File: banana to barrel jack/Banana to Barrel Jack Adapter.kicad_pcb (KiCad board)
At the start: 2 copper layers, 34.3 x 26.6 mm, 29 parts, among them J1 USB_A, J2 Positive, J3 Negative, J4 Data

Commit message: Zone Relief DRC error in PCB
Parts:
- removed ? (x7): , 
- removed J4: Data, Connector_PinHeader_2.54mm:PinHeader_1x02_P2.54mm_Vertical
- removed the REF** at (133.1, 98.6)
- removed the REF** at (127.3, 99.5)
- removed the REF** at (133.1, 100.8)
- removed the REF** at (133.1, 102.0)
- removed the REF** at (129.6, 99.5)
- removed the REF** at (131.9, 99.5)
- removed the REF** at (133.1, 97.6)
- removed the REF** at (133.1, 99.6)
- removed the REF** at (130.8, 99.5)
- removed the REF** at (133.1, 103.1)
- removed the REF** at (133.1, 96.5)
- removed the REF** at (128.5, 99.5)
- removed the REF** at (126.1, 99.5)
- added D2: Green, LED_SMD:LED_1206_3216Metric_Pad1.42x1.75mm_HandSolder, B.Cu at (146.8, 96.9)
- added R2: 1k, Resistor_SMD:R_1206_3216Metric_Pad1.30x1.75mm_HandSolder, B.Cu at (146.8, 102.3)
- added REF**: Symbol_Barrel_Polarity, Symbol:Symbol_Barrel_Polarity, F.Cu at (151.2, 106.4)
- added REF**: Symbol_Barrel_Polarity, Symbol:Symbol_Barrel_Polarity, B.Cu at (151.2, 106.2)
- J1: value USB_A -> Barrel_Jack_Switch; footprint My Libraries:USB_A_GCT_USB1125 -> Connector_BarrelJack:BarrelJack_GCT_DCJ200-10-A_Horizontal
- moved J1 4.44 mm to (151.7, 98.8)
- moved D3 1.93 mm to (154.8, 99.5)
- renumbered D2 to D3
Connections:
- J1 pad 2: Net-(J1-D-) -> GND
- J1 pad 3: Net-(J1-D+) -> GND
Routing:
- net /Positive: track 0.00 -> 7.05 mm
- net Net-(J1-D-): track 3.53 -> 0.00 mm
- net Net-(J1-D+): track 3.52 -> 0.00 mm

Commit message: 0 DRC before changing zones for positive
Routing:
- net /Positive: track 7.05 -> 0.00 mm
- net Net-(D2-A): track 0.00 -> 2.31 mm
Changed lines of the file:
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@@
 		)
 		(model "${KICAD8_3DMODEL_DIR}/Connector_BarrelJack.3dshapes/BarrelJack_GCT_DCJ200-10-A_Horizontal.wrl"
+			(hide yes)
 			(offset
 				(xyz 0 0 0)
@@
 			)
 		)
+		(model "${KICAD8_3DMODEL_DIR}/Connector_BarrelJack.3dshapes/BarrelJack_Horizontal.step"
+			(offset
+				(xyz 0 0 0)
+			)
+			(scale
+				(xyz 1 1 1)
+			)
+			(rotate
+				(xyz 0 0 -90)
+			)
+		)
 	)
 	(footprint "Connector_PinHeader_2.54mm:PinHeader_1x01_P2.54mm_Vertical"
@@
 		)
 	)
+	(gr_rect
+		(start 127.75 95.75)
+		(end 129.05 95.65)
+		(stroke
+			(width 0)
+			(type solid)
+		)
+		(fill solid)
+		(layer "B.SilkS")
+	)
+	(gr_rect
+		(start 127.75 96.85)
+		(end 129.05 96.75)
+		(stroke
+			(width 0)
+			(type solid)
+		)
+		(fill solid)
+		(layer "B.SilkS")
+	)
 	(gr_line
 		(start 131.725 95.925)
@@
 		(layer "B.SilkS")
 	)
+	(gr_rect
+		(start 127.75 96.825)
+		(end 128.2 95.675)
+		(stroke
+			(width 0)
+			(type solid)
+		)
+		(fill solid)
+		(layer "B.SilkS")
+	)
+	(gr_rect
+		(start 146.85 90.9)
+		(end 147.55 88.75)
+		(stroke
+			(width 0)
+			(type solid)
+		)
+		(fill solid)
+		(layer "B.SilkS")
+	)
+	(gr_rect
+		(start 128.55 96.825)
+		(end 129.05 95.675)
+		(stroke
+			(width 0)
+			(type solid)
+		)
+		(fill solid)
+		(layer "B.SilkS")
+	)
 	(gr_line
 		(start 131.725 102.85)
@@
 		(layer "B.SilkS")
 	)
+	(gr_rect
+		(start 148.1 90.9)
+		(end 148.8 88.75)
+		(stroke
+			(width 0)
+			(type solid)
+		)
+		(fill solid)
+		(layer "B.SilkS")
+	)
+	(gr_rect
+		(start 146.85 90.9)
+		(end 148.75 90.7)
+		(stroke
+			(width 0)
+			(type solid)
+		)
+		(fill solid)
+		(layer "B.SilkS")
+	)
+	(gr_rect
+		(start 146.85 88.95)
+		(end 148.75 88.75)
+		(stroke
+			(width 0)
+			(type solid)
+		)
+		(fill solid)
+		(layer "B.SilkS")
+	)
 	(gr_line
 		(start 131.725 102.825)
@@
 		(layer "B.SilkS")
 	)
+	(gr_rect
+		(start 128.6 95.675)
+		(end 129.05 96.825)
+		(stroke
+			(width 0)
+			(type solid)
+		)
+		(fill solid)
+		(layer "F.SilkS")
+	)
+	(gr_rect
+		(start 146.9 90.7)
+		(end 148.8 90.9)
+		(stroke
+			(width 0)
+			(type solid)
+		)
+		(fill solid)
+		(layer "F.SilkS")
+	)
+	(gr_rect
+		(start 127.75 95.65)
+		(end 129.05 95.75)
+		(stroke
+			(width 0)
+			(type solid)
+		)
+		(fill solid)
+		(layer "F.SilkS")
+	)
+	(gr_rect
+		(start 127.75 95.675)
+		(end 128.25 96.825)
+		(stroke
+			(width 0)
+			(type solid)
+		)
+		(fill solid)
+		(layer "F.SilkS")
+	)
 	(gr_line
 		(start 139.575 103.075)
@@
 		(layer "F.SilkS")
 	)
+	(gr_rect
+		(start 127.75 96.75)
+		(end 129.05 96.85)
+		(stroke
+			(width 0)
+			(type solid)
+		)
+		(fill solid)
+		(layer "F.SilkS")
+	)
 	(gr_circle
 		(center 131.75 103.025)
@@
 		(layer "F.SilkS")
 	)
+	(gr_rect
+		(start 146.9 88.75)
+		(end 148.8 88.95)
+		(stroke
+			(width 0)
+			(type solid)
+		)
+		(fill solid)
+		(layer "F.SilkS")
+	)
 	(gr_line
 		(start 139.575 103.075)
@@
 		(layer "F.SilkS")
 	)
+	(gr_rect
+		(start 148.1 88.75)
+		(end 148.8 90.9)
+		(stroke
+			(width 0)
+			(type solid)
+		)
+		(fill solid)
+		(layer "F.SilkS")
+	)
 	(gr_line
 		(start 139.4 103.25)
@@
 		(layer "F.SilkS")
 	)
+	(gr_rect
+		(start 146.85 88.75)
+		(end 147.55 90.9)
+		(stroke
+			(width 0)
+			(type solid)
+		)
+		(fill solid)
+		(layer "F.SilkS")
+	)
 	(gr_line
 		(start 139.4 102.9)
@@
 	)
 	(gr_text "-"
-		(at 128.4895 96.26765 -90)
+		(at 128.4895 96.25 -90)
 		(layer "B.SilkS" knockout)
 		(effects
@@
 	)
 	(gr_text "+"
-		(at 128.4895 102.703 0)
+		(at 128.4895 102.65 0)
 		(layer "B.SilkS" knockout)
 		(effects
@@
 	)
 	(gr_text "-"
-		(at 149.1742 91.166995 90)
+		(at 148.85 91.15 90)
 		(layer "F.SilkS" knockout)
 		(effects
@@
 	)
 	(gr_text "+"
-		(at 146.761105 110.1789 0)
+		(at 146.55 110.1789 0)
 		(layer "F.SilkS" knockout)
 		(effects
@@
 	)
 	(gr_text "-"
-		(at 128.4895 96.221425 90)
+		(at 128.35 96.25 90)
 		(layer "F.SilkS" knockout)
 		(effects
@@
 		(net 1)
 	)
-	(segment
-		(start 149.89325 100.6458)
-		(end 153.0255 100.6458)
-		(width 0.25)
-		(layer "F.Cu")
-		(net 2)
-	)
-	(segment
-		(start 153.0255 100.6458)
-		(end 153.3065 100.3648)
-		(width 0.25)
-		(layer "F.Cu")
-		(net 2)
-	)
-	(segment
-		(start 149.89325 98.1058)
-		(end 153.0475 98.1058)
-		(width 0.25)
-		(layer "F.Cu")
-		(net 2)
-	)
-	(segment
-		(start 153.0475 98.1058)
-		(end 153.3065 98.3648)
-		(width 0.25)
-		(layer "F.Cu")
-		(net 2)
-	)
 	(via
 		(at 144.8562 110.53572)
@@
 		(net 3)
 	)
+	(segment
+		(start 146.79 98.4075)
+		(end 146.79 100.72)
+		(width 0.5)
+		(layer "B.Cu")
+		(net 4)
+	)
 	(zone
 		(net 2)
@@
 		)
 	)
+	(group ""
+		(members "03433355-6bb3-446d-9a6d-a2e5b72d6f9c" "07b327e9-676c-4b22-8802-34a8a017ee86"
+			"812e787f-b3ed-41a6-bb3a-bdb902afadbf" "8b55572f-fa6a-4e7c-b22f-9cf51528f95c"
+		)
+	)
+	(group ""
+		(members "876096bc-b1d5-4e9a-9cdb-3daaf280bf9d" "9402d68d-7a4b-4ece-86ce-f0ebfa78f54e"
+			"a5ec77df-c86e-444f-92c5-92dc659a62b3" "b2f959b1-7101-4a8c-b801-1e8fdb9a2005"
+		)
+	)
+	(group ""
+		(members "22873648-8d8c-450a-9397-42385f8aac2b" "9b107eb4-2d82-42f6-b674-1bb251eae402"
+			"c5bfd072-bf1a-4381-a8b1-2d2add5322a2" "e6739268-a3a3-4171-aaab-85ea9d387f7c"
+		)
+	)
+	(group ""
+		(members "12e7e9ea-4806-45f0-af63-483ef2b5ac83" "32d8726d-c00d-4061-87aa-49370713e9ea"
+			"35eebb64-d20b-4ada-b715-29849750b198" "722da3e9-53a3-4bcb-9cbf-1dace17913f2"
+		)
+	)

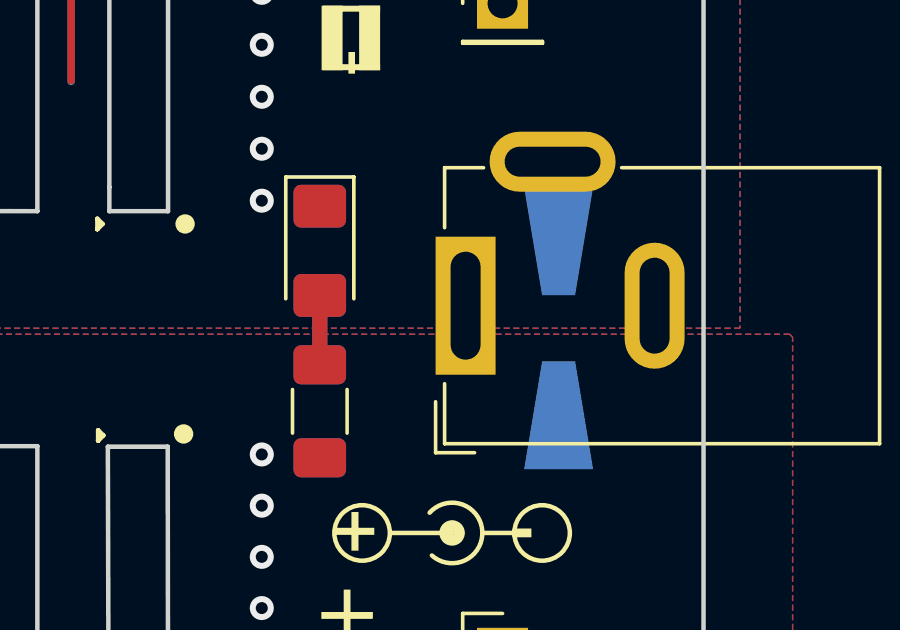
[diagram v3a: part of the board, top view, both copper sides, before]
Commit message: DRC warning about footprints not matching library. going to try and update all.
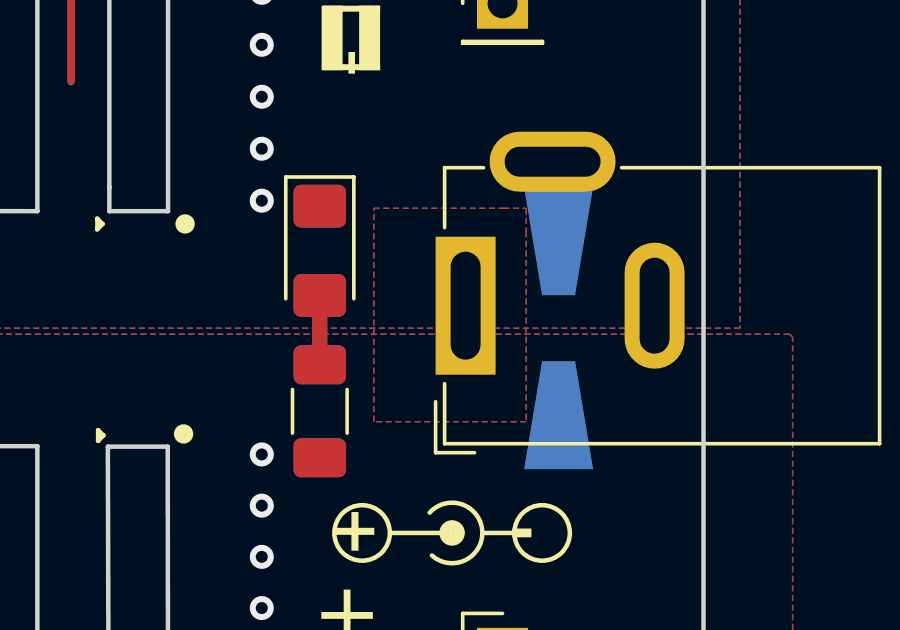
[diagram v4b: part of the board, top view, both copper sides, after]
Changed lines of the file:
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@@
+	)
+	(zone
+		(net 2)
+		(net_name "/Positive")
+		(layers "F&B.Cu")
+		(hatch edge 0.5)
+		(priority 1)
+		(connect_pads
+			(clearance 0)
+		)
+		(min_thickness 0.25)
+		(filled_areas_thickness no)
+		(fill yes
+			(thermal_gap 0.254)
+			(thermal_bridge_width 5)
+		)
+		(polygon
+			(pts
+				(xy 148.59 95.504) (xy 152.908 95.504) (xy 153.67 95.504) (xy 153.67 96.266) (xy 153.67 102.616)
+				(xy 148.59 102.616)
+			)
+		)
 	)
 	(zone
@@
 			)
 		)
-	)
-	(zone
-		(net 0)
-		(net_name "")
-		(layers "F&B.Cu")
-		(hatch edge 0.508)
-		(connect_pads
-			(clearance 0)
-		)
-		(min_thickness 0.254)
-		(filled_areas_thickness no)
-		(keepout
-			(tracks allowed)
-			(vias allowed)
-			(pads allowed)
-			(copperpour not_allowed)
-			(footprints allowed)
-		)
-		(fill
-			(thermal_gap 0.254)
-			(thermal_bridge_width 1.016)
-			(island_removal_mode 2)
-			(island_area_min 10)
-		)
-		(polygon
-			(pts
-				(xy 158.6992 98.4758) (xy 145.7 98.4758) (xy 145.7 100.26881) (xy 158.623 100.2538) (xy 158.6992 100.1776)
-			)
-		)
